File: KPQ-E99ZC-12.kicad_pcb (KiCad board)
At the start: 2 copper layers, 79 x 50.7 mm, 23 parts, among them J1 USB, J2 Chassis, J3 SWD, J4 Edge Connector, J5 Alternate Connector, SW1 BOOT, U1 USBLC6-2SC6, U2 XC6206P332MR-G, U3 STM32C071KBT6

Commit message: Minor tweaks
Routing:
- net GND: vias 16 -> 17
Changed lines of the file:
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@@
 			(psa4output no)
 			(plot_black_and_white yes)
-			(plotinvisibletext no)
 			(sketchpadsonfab no)
 			(plotpadnumbers no)
@@
 		(tags "Through hole pin header THT 1x04 2.54mm single row")
 		(property "Reference" "J1"
-			(at 0 -3.302 0)
+			(at 3.5 3.810001 90)
 			(layer "F.SilkS")
+			(hide yes)
 			(effects
 				(font
@@
 		)
 		(property "Value" "USB"
-			(at 0 10.922 0)
+			(at -0.3125 -3.302 0)
 			(layer "F.SilkS")
 			(effects
@@
 					(thickness 0.15)
 				)
+				(justify left)
 			)
 		)
@@
 		(sheetfile "KPQ-E99ZC-12.kicad_sch")
 		(attr through_hole)
-		(fp_rect
-			(start -1.33 -2.44)
+		(fp_line
+			(start 0 -2.44)
+			(end 0 -1)
+			(stroke
+				(width 0.1)
+				(type solid)
+			)
+			(layer "F.SilkS")
+		)
+		(fp_line
+			(start 0 1.54)
+			(end 0 1)
+			(stroke
+				(width 0.1)
+				(type solid)
+			)
+			(layer "F.SilkS")
+		)
+		(fp_line
+			(start 0 4.08)
+			(end 0 3.54)
+			(stroke
+				(width 0.1)
+				(type solid)
+			)
+			(layer "F.SilkS")
+		)
+		(fp_line
+			(start 0 6.62)
+			(end 0 6.08)
+			(stroke
+				(width 0.1)
+				(type solid)
+			)
+			(layer "F.SilkS")
+		)
+		(fp_line
+			(start 0 10.033)
+			(end 0 8.62)
+			(stroke
+				(width 0.1)
+				(type solid)
+			)
+			(layer "F.SilkS")
+		)
+		(fp_line
+			(start 7 -2.44)
+			(end 0 -2.44)
+			(stroke
+				(width 0.1)
+				(type solid)
+			)
+			(layer "F.SilkS")
+		)
+		(fp_line
+			(start 7 -2.44)
 			(end 7 10.06)
 			(stroke
 				(width 0.1)
+				(type default)
+			)
+			(layer "F.SilkS")
+		)
+		(fp_line
+			(start 7 10.06)
+			(end 0 10.06)
+			(stroke
+				(width 0.1)
 				(type solid)
 			)
-			(fill no)
 			(layer "F.SilkS")
 		)
 		(fp_rect
-			(start -1.8 -2.871)
+			(start -1.292 -2.871)
 			(end 7.47 10.469)
 			(stroke
@@
 		)
 		(fp_text user "${P1}"
-			(at 9.144 0 0)
+			(at 7.512 0 0)
 			(layer "F.SilkS")
 			(effects
@@
 					(bold yes)
 				)
+				(justify left)
 			)
 		)
 		(fp_text user "${P2}"
-			(at 9.144 2.54 0)
+			(at 7.512 2.54 0)
 			(layer "F.SilkS")
 			(effects
@@
 					(bold yes)
 				)
+				(justify left)
 			)
 		)
 		(fp_text user "${P4}"
-			(at 9.144 7.62 0)
+			(at 7.512 7.62 0)
 			(layer "F.SilkS")
 			(effects
@@
 					(bold yes)
 				)
+				(justify left)
 			)
 		)
 		(fp_text user "${P3}"
-			(at 9.144 5.08 0)
+			(at 7.512 5.08 0)
 			(layer "F.SilkS")
 			(effects
@@
 					(bold yes)
 				)
+				(justify left)
 			)
 		)
@@
 			(at 0 -2.35 0)
 			(layer "F.SilkS")
+			(hide yes)
 			(effects
 				(font
@@
 			)
 		)
-		(pad "1" thru_hole roundrect
+		(pad "1" thru_hole circle
 			(at 0 0)
-			(size 2.3 2.3)
+			(size 2.7 2.7)
 			(drill 1.1)
 			(layers "*.Cu" "*.Mask")
 			(remove_unused_layers no)
-			(roundrect_rratio 0.108696)
 			(net 1 "GND")
 			(pinfunction "Pin_1")
 			(pintype "passive")
+			(thermal_bridge_width 0.2)
+			(thermal_gap 1)
 		)
 		(embedded_fonts no)
@@
 			(at 0 -2.33 90)
 			(layer "F.SilkS")
+			(hide yes)
 			(effects
 				(font
@@
 			(at 0 -2.33 180)
 			(layer "F.SilkS")
+			(hide yes)
 			(effects
 				(font
@@
 			(at 0 3.599999 90)
 			(layer "B.SilkS")
+			(hide yes)
 			(effects
 				(font
@@
 	)
 	(via
-		(at 121.271 122.606)
+		(at 121.906 122.733)
 		(size 0.8)
 		(drill 0.5)
@@
 		(net 1)
 	)
+	(via
+		(at 128.067 120.8)
+		(size 0.5)
+		(drill 0.3)
+		(layers "F.Cu" "B.Cu")
+		(free yes)
+		(net 1)
+	)
 	(segment
 		(start 102 128)
@@
 	)
 	(segment
-		(start 125.249 120.8)
-		(end 129.031 117.018)
+		(start 123.255905 144.13955)
+		(end 123.255905 143.31045)
 		(width 0.4)
 		(layer "F.Cu")
@@
 	)
 	(segment
-		(start 122.541 120.8)
-		(end 125.249 120.8)
+		(start 129.031 117.018)
+		(end 128.891 113)
 		(width 0.4)
 		(layer "F.Cu")
@@
 	)
 	(segment
-		(start 123.255905 144.13955)
-		(end 123.255905 143.31045)
+		(start 129.031 117.705)
+		(end 129.031 117.018)
 		(width 0.4)
 		(layer "F.Cu")
@@
 	)
 	(segment
-		(start 129.031 117.018)
-		(end 128.891 113)
+		(start 108.031 117.018)
+		(end 107.891 113)
 		(width 0.4)
 		(layer "F.Cu")
@@
 	)
 	(segment
-		(start 108.031 117.018)
-		(end 107.891 113)
+		(start 117.427001 146.630355)
+		(end 116.016 146.630355)
 		(width 0.4)
 		(layer "F.Cu")
@@
 	)
 	(segment
-		(start 117.427001 146.630355)
-		(end 116.016 146.630355)
+		(start 122.541 120.8)
+		(end 125.936 120.8)
 		(width 0.4)
 		(layer "F.Cu")
@@
 	)
 	(segment
+		(start 125.936 120.8)
+		(end 129.031 117.705)
+		(width 0.4)
+		(layer "F.Cu")
+		(net 2)
+	)
+	(segment
 		(start 108.031 120.8)
 		(end 108.031 117.018)
@@
 	)
 	(segment
-		(start 106.221 125.825)
+		(start 104.318 125.825)
 		(end 102.8 125.825)
 		(width 0.2)
@@
 	)
 	(via
-		(at 106.221 125.825)
+		(at 104.318 125.825)
 		(size 0.5)
 		(drill 0.3)
@@
 	)
 	(segment
-		(start 106.221 125.825)
-		(end 125.136 125.825)
+		(start 130.161 120.8)
+		(end 130.161 113)
 		(width 0.2)
 		(layer "B.Cu")
@@
 	)
 	(segment
-		(start 130.161 120.8)
-		(end 130.161 113)
+		(start 125.136 125.825)
+		(end 130.161 120.8)
 		(width 0.2)
 		(layer "B.Cu")
@@
 	)
 	(segment
-		(start 125.136 125.825)
-		(end 130.161 120.8)
+		(start 104.318 125.825)
+		(end 125.136 125.825)
 		(width 0.2)
 		(layer "B.Cu")

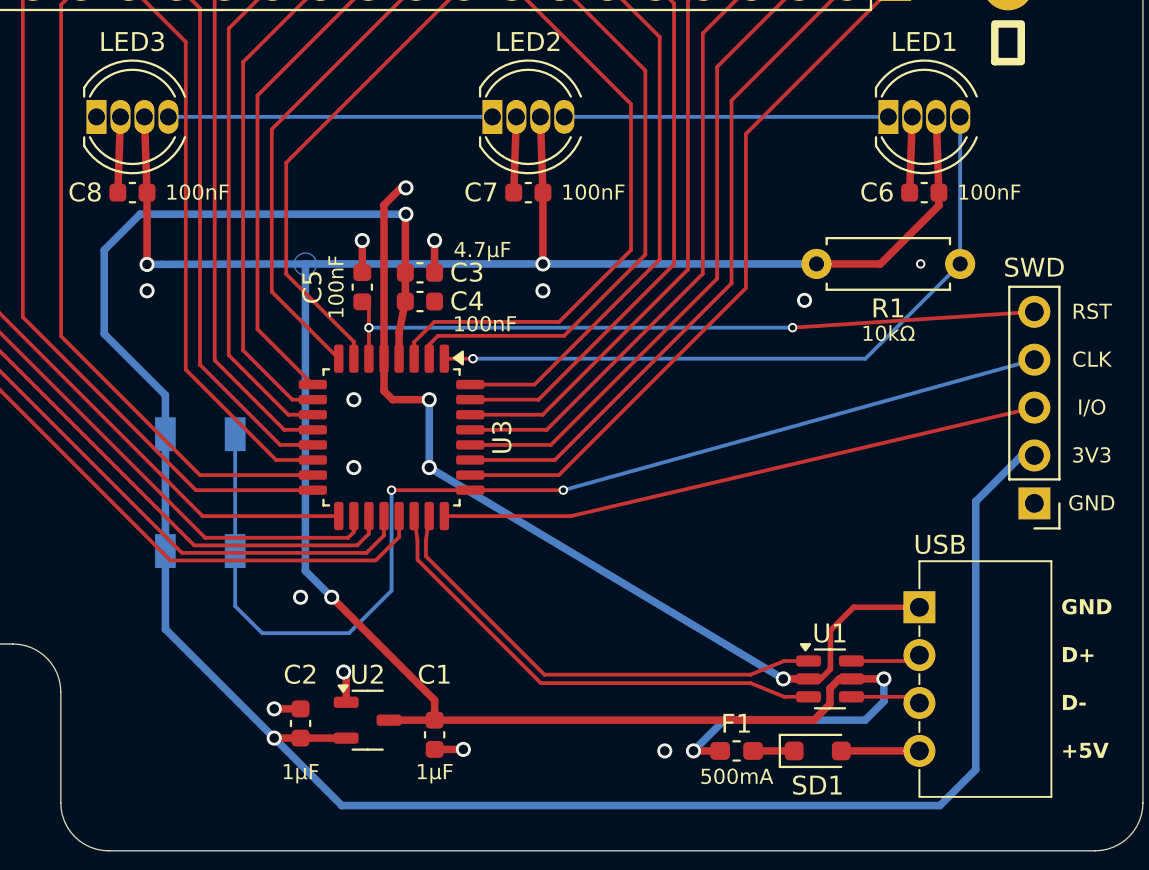
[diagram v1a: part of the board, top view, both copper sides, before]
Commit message: Add additional ground vias and tweak routing
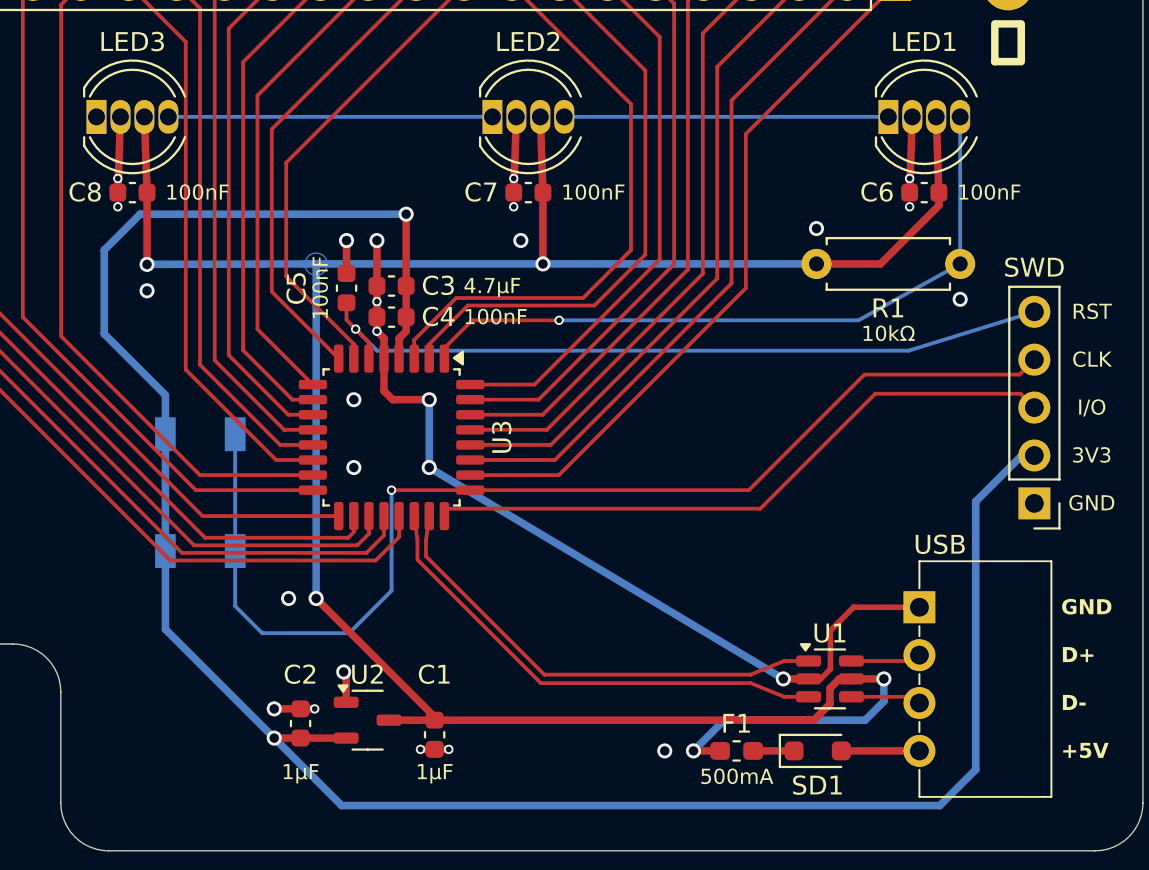
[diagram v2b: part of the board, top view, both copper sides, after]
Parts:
- moved C4 1.72 mm to (100.0, 123.6), turned to 180 degrees
- moved C3 1.66 mm to (100.0, 122.0), turned to 180 degrees
- moved C5 0.84 mm to (97.6, 122.1)
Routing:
- net GND: track 69.5 -> 65.3 mm, vias 17 -> 26
- net SWDIO: track 32.0 -> 34.1 mm
- net NRST: track 38.4 -> 40.3 mm, vias 2 -> 1
- net BOOT0/SWCLK: track 59.3 -> 61.3 mm, vias 2 -> 1
- net LED: track 37.2 -> 36.5 mm

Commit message: Add pin labelling to alternate connection
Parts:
- J3: footprint Connector_PinHeader_2.54mm:PinHeader_1x05_P2.54mm_Vertical -> Project_Library:PinHeader_1x05_P2.54mm_Vertical
- J5: footprint Connector_PinHeader_2.54mm:PinHeader_1x24_P2.54mm_Vertical -> Project_Library:PinHeader_1x24_P2.54mm_Vertical

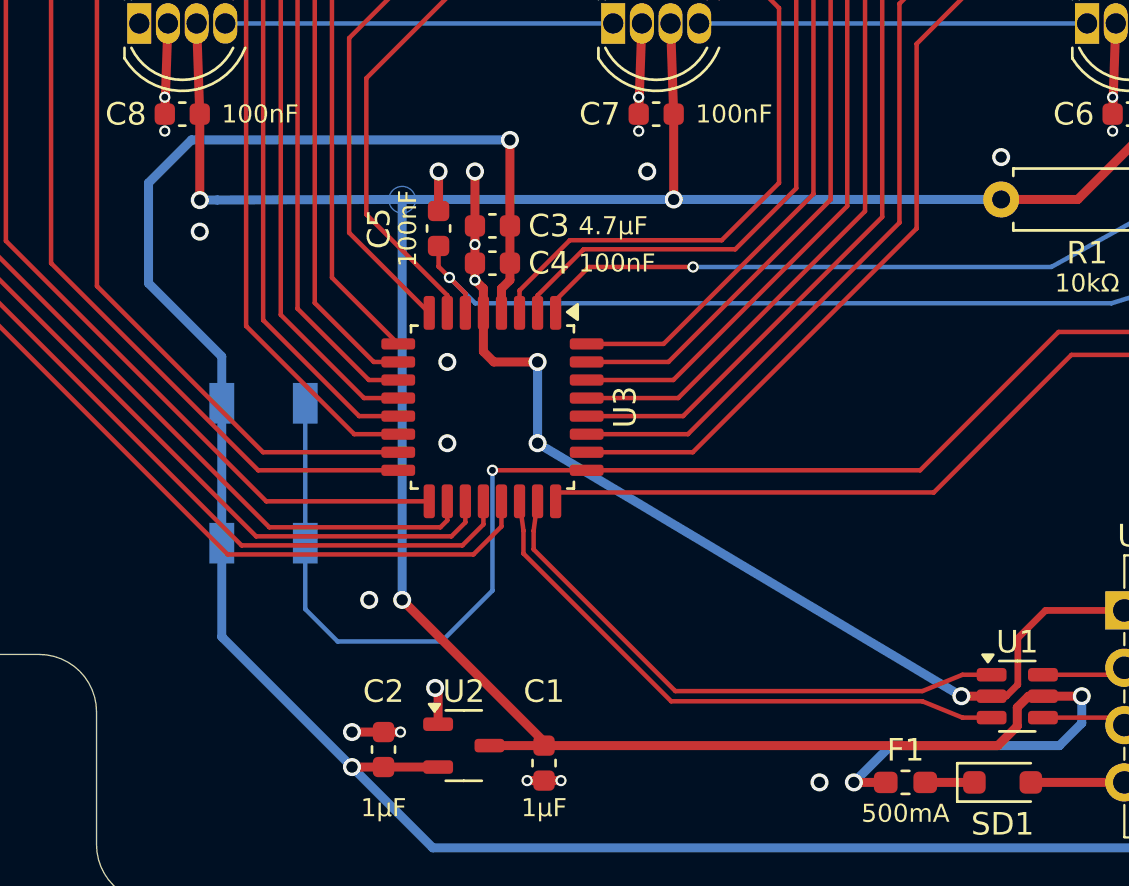
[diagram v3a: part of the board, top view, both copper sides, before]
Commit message: Round USB data lines; other routing tweaks
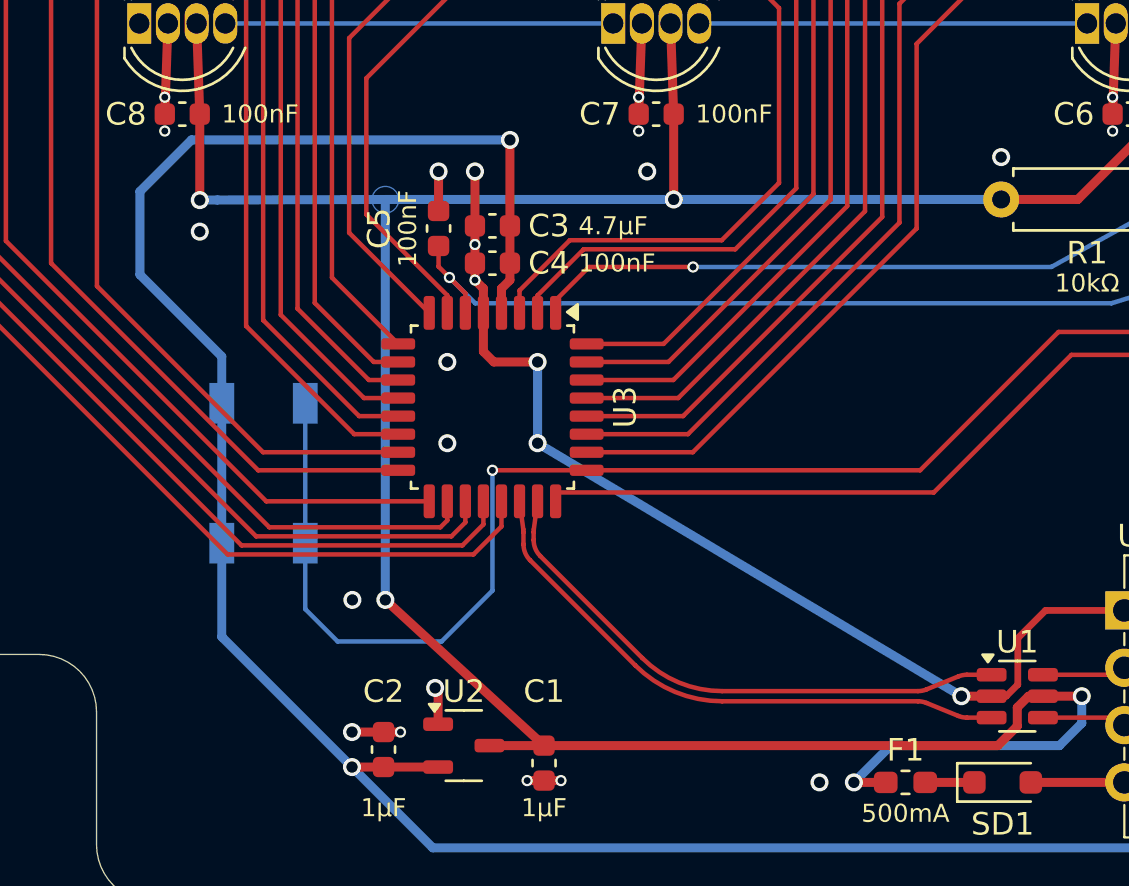
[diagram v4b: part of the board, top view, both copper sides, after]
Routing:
- net +5V: track 131.9 -> 132.5 mm
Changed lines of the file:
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@@
 	)
 	(via
-		(at 94.539 138.5445)
+		(at 93.793563 138.5445)
 		(size 0.8)
 		(drill 0.5)
@@
 	)
 	(segment
-		(start 102.286 144.831)
-		(end 95.9995 138.5445)
-		(width 0.4)
-		(layer "F.Cu")
-		(net 2)
-	)
-	(segment
 		(start 102.286 145)
 		(end 102.286 144.831)
@@
 		(start 125.936 120.8)
 		(end 129.031 117.705)
+		(width 0.4)
+		(layer "F.Cu")
+		(net 2)
+	)
+	(segment
+		(start 95.254063 138.5445)
+		(end 102.286 145)
 		(width 0.4)
 		(layer "F.Cu")
@@
 	)
 	(via
-		(at 95.9995 138.5445)
+		(at 95.254063 138.5445)
 		(size 0.8)
 		(drill 0.5)
@@
 	)
 	(segment
-		(start 95.9995 120.8)
-		(end 95.9995 138.5445)
+		(start 95.254063 120.8)
+		(end 95.254063 138.5445)
 		(width 0.4)
 		(layer "B.Cu")
@@
 	)
 	(segment
+		(start 88.005999 127.756999)
+		(end 84.379 124.13)
+		(width 0.4)
+		(layer "B.Cu")
+		(net 3)
+	)
+	(segment
+		(start 97.357 149.53)
+		(end 129.083 149.53)
+		(width 0.4)
+		(layer "B.Cu")
+		(net 3)
+	)
+	(segment
+		(start 86.665 118.161)
+		(end 100.762 118.161)
+		(width 0.4)
+		(layer "B.Cu")
+		(net 3)
+	)
+	(segment
+		(start 88.005999 129.83)
+		(end 88.005999 140.178999)
+		(width 0.4)
+		(layer "B.Cu")
+		(net 3)
+	)
+	(segment
+		(start 130.988 147.625)
+		(end 130.988 133.401)
+		(width 0.4)
+		(layer "B.Cu")
+		(net 3)
+	)
+	(segment
+		(start 84.379 124.13)
+		(end 84.379 120.447)
+		(width 0.4)
+		(layer "B.Cu")
+		(net 3)
+	)
+	(segment
+		(start 133.429 130.96)
+		(end 134.096 130.96)
+		(width 0.4)
+		(layer "B.Cu")
+		(net 3)
+	)
+	(segment
 		(start 88.005999 129.83)
 		(end 88.005999 127.756999)
@@
 	)
 	(segment
-		(start 97.357 149.53)
-		(end 129.083 149.53)
-		(width 0.4)
-		(layer "B.Cu")
-		(net 3)
-	)
-	(segment
-		(start 84.76 120.066)
+		(start 84.379 120.447)
 		(end 86.665 118.161)
-		(width 0.4)
-		(layer "B.Cu")
-		(net 3)
-	)
-	(segment
-		(start 88.005999 129.83)
-		(end 88.005999 140.178999)
-		(width 0.4)
-		(layer "B.Cu")
-		(net 3)
-	)
-	(segment
-		(start 130.988 147.625)
-		(end 130.988 133.401)
-		(width 0.4)
-		(layer "B.Cu")
-		(net 3)
-	)
-	(segment
-		(start 86.665 118.161)
-		(end 100.762 118.161)
-		(width 0.4)
-		(layer "B.Cu")
-		(net 3)
-	)
-	(segment
-		(start 84.76 124.511)
-		(end 84.76 120.066)
-		(width 0.4)
-		(layer "B.Cu")
-		(net 3)
-	)
-	(segment
-		(start 88.005999 127.756999)
-		(end 84.76 124.511)
-		(width 0.4)
-		(layer "B.Cu")
-		(net 3)
-	)
-	(segment
-		(start 133.429 130.96)
-		(end 134.096 130.96)
 		(width 0.4)
 		(layer "B.Cu")
@@
 	)
 	(segment
-		(start 107.919157 143.035355)
-		(end 119.05 143.035355)
+		(start 110.176621 143.035355)
+		(end 118.853955 143.035355)
 		(width 0.2)
 		(layer "F.Cu")
@@
 	)
 	(segment
-		(start 120.828 143.760355)
+		(start 121.024045 143.760355)
 		(end 122.1185 143.760355)
 		(width 0.2)
@@
 	)
 	(segment
-		(start 101.375 135.475001)
-		(end 101.375 136.491198)
+		(start 101.375 135.542006)
+		(end 101.375 136.076984)
 		(width 0.2)
 		(layer "F.Cu")
@@
 	)
 	(segment
-		(start 101.375 136.491198)
-		(end 107.919157 143.035355)
+		(start 101.667893 136.784091)
+		(end 106.322889 141.439087)
 		(width 0.2)
 		(layer "F.Cu")
@@
 	(segment
 		(start 101.2 134.175)
-		(end 101.375 135.475001)
+		(end 101.366061 135.408594)
 		(width 0.2)
 		(layer "F.Cu")
@@
 	)
 	(segment
-		(start 119.05 143.035355)
-		(end 120.828 143.760355)
+		(start 119.231533 143.109377)
+		(end 120.646467 143.686333)
 		(width 0.2)
 		(layer "F.Cu")
 		(net 38)
 	)
+	(arc
+		(start 121.024045 143.760355)
+		(mid 120.831662 143.741675)
+		(end 120.646467 143.686333)
+		(width 0.2)
+		(layer "F.Cu")
+		(net 38)
+	)
+	(arc
+		(start 118.853955 143.035355)
+		(mid 119.046338 143.054035)
+		(end 119.231533 143.109377)
+		(width 0.2)
+		(layer "F.Cu")
+		(net 38)
+	)
+	(arc
+		(start 101.375 135.542006)
+		(mid 101.372763 135.47515)
+		(end 101.366061 135.408594)
+		(width 0.2)
+		(layer "F.Cu")
+		(net 38)
+	)
+	(arc
+		(start 101.375 136.076984)
+		(mid 101.45112 136.459667)
+		(end 101.667893 136.784091)
+		(width 0.2)
+		(layer "F.Cu")
+		(net 38)
+	)
+	(arc
+		(start 110.176621 143.035355)
+		(mid 108.090996 142.620498)
+		(end 106.322889 141.439087)
+		(width 0.2)
+		(layer "F.Cu")
+		(net 38)
+	)
 	(segment
 		(start 102 134.175)
-		(end 101.825 135.475001)
+		(end 101.833939 135.408594)
 		(width 0.2)
 		(layer "F.Cu")
@@
 	)
 	(segment
-		(start 101.825 136.304802)
-		(end 108.105553 142.585355)
+		(start 102.117893 136.597695)
+		(end 106.641087 141.120889)
 		(width 0.2)
 		(layer "F.Cu")
@@
 	)
 	(segment
-		(start 108.105553 142.585355)
-		(end 119.05 142.585355)
+		(start 110.176621 142.585355)
+		(end 118.853955 142.585355)
 		(width 0.2)
 		(layer "F.Cu")
@@
 	)
 	(segment
-		(start 101.825 135.475001)
-		(end 101.825 136.304802)
+		(start 101.825 135.542006)
+		(end 101.825 135.890588)
 		(width 0.2)
 		(layer "F.Cu")
@@
 	)
 	(segment
-		(start 120.828 141.860355)
+		(start 121.024045 141.860355)
 		(end 122.1185 141.860355)
 		(width 0.2)
@@
 	)
 	(segment
-		(start 119.05 142.585355)
-		(end 120.828 141.860355)
+		(start 119.231533 142.511333)
+		(end 120.646467 141.934377)
+		(width 0.2)
+		(layer "F.Cu")
+		(net 39)
+	)
+	(arc
+		(start 106.641087 141.120889)
+		(mid 108.263204 142.204753)
+		(end 110.176621 142.585355)
+		(width 0.2)
+		(layer "F.Cu")
+		(net 39)
+	)
+	(arc
+		(start 121.024045 141.860355)
+		(mid 120.831662 141.879035)
+		(end 120.646467 141.934377)
+		(width 0.2)
+		(layer "F.Cu")
+		(net 39)
+	)
+	(arc
+		(start 102.117893 136.597695)
+		(mid 101.90112 136.273272)
+		(end 101.825 135.890588)
+		(width 0.2)
+		(layer "F.Cu")
+		(net 39)
+	)
+	(arc
+		(start 118.853955 142.585355)
+		(mid 119.046338 142.566675)
+		(end 119.231533 142.511333)
+		(width 0.2)
+		(layer "F.Cu")
+		(net 39)
+	)
+	(arc
+		(start 101.833939 135.408594)
+		(mid 101.827237 135.47515)
+		(end 101.825 135.542006)
 		(width 0.2)
 		(layer "F.Cu")
@@
 		(polygon
 			(pts
-				(xy 96.587563 120.734211) (xy 96.547487 120.584647) (xy 96.470067 120.450552) (xy 96.360579 120.341064)
-				(xy 96.226484 120.263644) (xy 96.07692 120.223568) (xy 95.92208 120.223568) (xy 95.772516 120.263644)
-				(xy 95.638421 120.341064) (xy 95.528933 120.450552) (xy 95.451513 120.584647) (xy 95.411437 120.734211)
-				(xy 95.411437 120.889051) (xy 95.451513 121.038615) (xy 95.528933 121.17271) (xy 95.638421 121.282198)
-				(xy 95.772516 121.359618) (xy 95.92208 121.399694) (xy 96.07692 121.399694) (xy 96.226484 121.359618)
-				(xy 96.360579 121.282198) (xy 96.470067 121.17271) (xy 96.547487 121.038615) (xy 96.587563 120.889051)
+				(xy 95.842126 120.734211) (xy 95.80205 120.584647) (xy 95.72463 120.450552) (xy 95.615142 120.341064)
+				(xy 95.481047 120.263644) (xy 95.331483 120.223568) (xy 95.176643 120.223568) (xy 95.027079 120.263644)
+				(xy 94.892984 120.341064) (xy 94.783496 120.450552) (xy 94.706076 120.584647) (xy 94.666 120.734211)
+				(xy 94.666 120.889051) (xy 94.706076 121.038615) (xy 94.783496 121.17271) (xy 94.892984 121.282198)
+				(xy 95.027079 121.359618) (xy 95.176643 121.399694) (xy 95.331483 121.399694) (xy 95.481047 121.359618)
+				(xy 95.615142 121.282198) (xy 95.72463 121.17271) (xy 95.80205 121.038615) (xy 95.842126 120.889051)
 			)
 		)
